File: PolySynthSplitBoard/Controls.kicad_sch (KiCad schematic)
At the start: 104 parts, among them SW601 ENV1_B, SW602 ENV2_B, SW603 HP_B, SW604 LFO1_B, SW605 LFO2_B, SW606 HP_B, SW607 LFO3_B, SW608 FF_B, SW609 MIX1_B, SW610 MIX2_B, SW611 ENC_MENU, SW612 ALT_B, U601 MCP23S17_SS, U602 MCP23S17_SS, U603 ILI9341

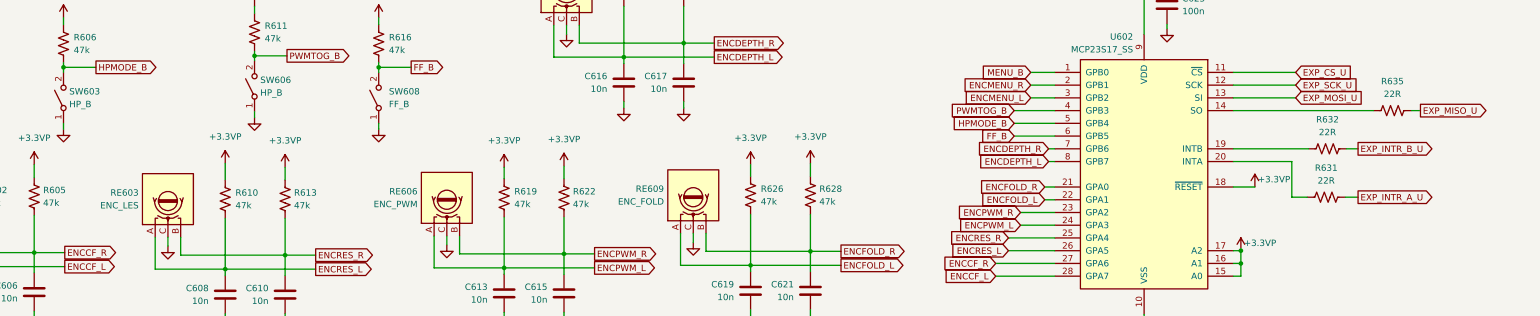
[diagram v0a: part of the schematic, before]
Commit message: upper board routing
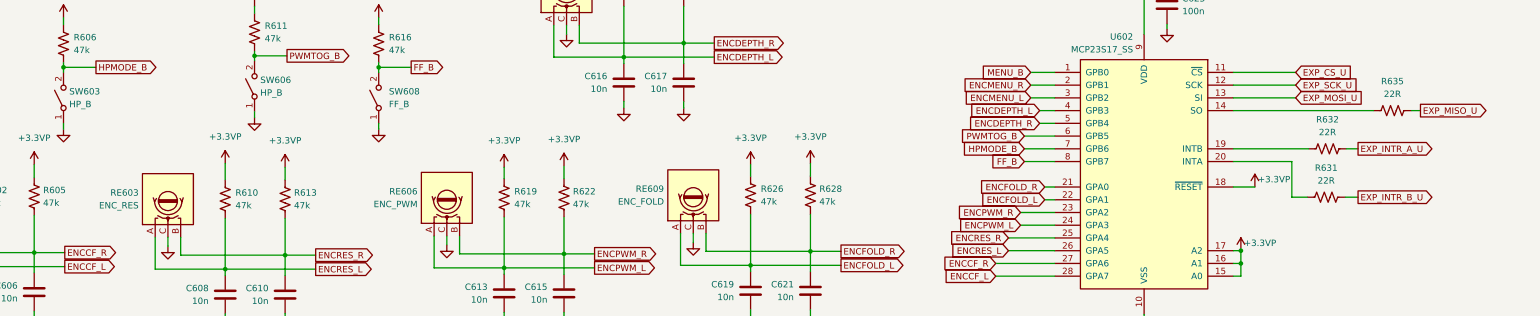
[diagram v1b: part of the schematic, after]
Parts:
- RE603: value ENC_LES -> ENC_RES
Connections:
- net ENCDEPTH_L: now also U602.4 (GPB3); no longer U602.8 (GPB7)
- net ENCDEPTH_R: now also U602.5 (GPB4); no longer U602.7 (GPB6)
- net EXP_INTR_A_U: now also R632.2; no longer R631.2
- net EXP_INTR_B_U: now also R631.2; no longer R632.2
- net FF_B: now also U602.8 (GPB7); no longer U602.6 (GPB5)
- net HPMODE_B: now also U602.7 (GPB6); no longer U602.5 (GPB4)
- net PWMTOG_B: now also U602.6 (GPB5); no longer U602.4 (GPB3)
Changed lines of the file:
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@@
 	(wire
 		(pts
-			(xy 246.634 183.896) (xy 254.762 183.896)
-		)
-		(stroke
-			(width 0)
-			(type default)
-		)
-	)
-	(wire
-		(pts
 			(xy 272.542 219.456) (xy 272.542 220.472)
 		)
@@
 	(wire
 		(pts
-			(xy 253.492 188.976) (xy 254.762 188.976)
-		)
-		(stroke
-			(width 0)
-			(type default)
-		)
-	)
-	(wire
-		(pts
 			(xy 224.79 83.312) (xy 229.108 83.312)
 		)
@@
 	(wire
 		(pts
+			(xy 248.666 186.436) (xy 254.762 186.436)
+		)
+		(stroke
+			(width 0)
+			(type default)
+		)
+	)
+	(wire
+		(pts
 			(xy 247.904 201.676) (xy 254.762 201.676)
 		)
@@
 	(wire
 		(pts
-			(xy 246.634 181.356) (xy 254.762 181.356)
+			(xy 251.714 181.356) (xy 254.762 181.356)
 		)
 		(stroke
@@
 	(wire
 		(pts
+			(xy 248.666 183.896) (xy 254.762 183.896)
+		)
+		(stroke
+			(width 0)
+			(type default)
+		)
+	)
+	(wire
+		(pts
 			(xy 175.26 101.346) (xy 175.26 107.696)
 		)
@@
 	(wire
 		(pts
+			(xy 248.666 188.976) (xy 254.762 188.976)
+		)
+		(stroke
+			(width 0)
+			(type default)
+		)
+	)
+	(wire
+		(pts
 			(xy 40.767 137.414) (xy 45.974 137.414)
 		)
@@
 	(wire
 		(pts
-			(xy 246.634 178.816) (xy 254.762 178.816)
+			(xy 251.714 178.816) (xy 254.762 178.816)
 		)
 		(stroke
@@
 	(wire
 		(pts
-			(xy 253.492 186.436) (xy 254.762 186.436)
-		)
-		(stroke
-			(width 0)
-			(type default)
-		)
-	)
-	(wire
-		(pts
 			(xy 322.326 83.82) (xy 322.326 85.598)
 		)
@@
 	(global_label "ENCDEPTH_R"
 		(shape input)
-		(at 253.492 186.436 180)
+		(at 251.714 181.356 180)
 		(fields_autoplaced yes)
 		(effects
@@
 		)
 		(property "Intersheetrefs" "${INTERSHEET_REFS}"
-			(at 238.7745 186.436 0)
+			(at 236.9965 181.356 0)
 			(effects
 				(font
@@
 	(global_label "ENCDEPTH_L"
 		(shape input)
-		(at 253.492 188.976 180)
+		(at 251.714 178.816 180)
 		(fields_autoplaced yes)
 		(effects
@@
 		)
 		(property "Intersheetrefs" "${INTERSHEET_REFS}"
-			(at 238.5326 188.976 0)
+			(at 236.7546 178.816 0)
 			(effects
 				(font
@@
 	(global_label "EXP_INTR_A_U"
 		(shape output)
-		(at 315.214 196.088 0)
+		(at 315.214 186.436 0)
 		(fields_autoplaced yes)
 		(effects
@@
 		)
 		(property "Intersheetrefs" "${INTERSHEET_REFS}"
-			(at 331.3225 196.088 0)
+			(at 331.3225 186.436 0)
 			(effects
 				(font
@@
 	(global_label "FF_B"
 		(shape input)
-		(at 246.634 183.896 180)
+		(at 248.666 188.976 180)
 		(fields_autoplaced yes)
 		(effects
@@
 		)
 		(property "Intersheetrefs" "${INTERSHEET_REFS}"
-			(at 239.234 183.896 0)
+			(at 241.266 188.976 0)
 			(effects
 				(font
@@
 	(global_label "EXP_INTR_B_U"
 		(shape output)
-		(at 315.214 186.436 0)
+		(at 315.214 196.088 0)
 		(fields_autoplaced yes)
 		(effects
@@
 		)
 		(property "Intersheetrefs" "${INTERSHEET_REFS}"
-			(at 331.5039 186.436 0)
+			(at 331.5039 196.088 0)
 			(effects
 				(font
@@
 	(global_label "PWMTOG_B"
 		(shape input)
-		(at 246.634 178.816 180)
+		(at 248.666 183.896 180)
 		(fields_autoplaced yes)
 		(effects
@@
 		)
 		(property "Intersheetrefs" "${INTERSHEET_REFS}"
-			(at 233.6703 178.816 0)
+			(at 235.7023 183.896 0)
 			(effects
 				(font
@@
 	(global_label "HPMODE_B"
 		(shape input)
-		(at 246.634 181.356 180)
+		(at 248.666 186.436 180)
 		(fields_autoplaced yes)
 		(effects
@@
 		)
 		(property "Intersheetrefs" "${INTERSHEET_REFS}"
-			(at 233.6098 181.356 0)
+			(at 235.6418 186.436 0)
 			(effects
 				(font
@@
 			)
 		)
-		(property "Value" "ENC_LES"
+		(property "Value" "ENC_RES"
 			(at 72.009 197.739 90)
 			(effects

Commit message: SPI and board tweaks
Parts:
- added C627: 10u, Capacitor_SMD:C_0805_2012Metric, symbol Device:C
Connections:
- net +3.3VP: now also C627.1
- net GNDA: now also C627.2
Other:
- moved on the sheet: C626
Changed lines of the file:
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@@
 	)
 	(junction
-		(at 363.728 27.178)
-		(diameter 0)
-		(color 0 0 0 0)
-	)
-	(junction
 		(at 88.519 63.5)
 		(diameter 0)
@@
 	)
 	(junction
+		(at 374.396 27.432)
+		(diameter 0)
+		(color 0 0 0 0)
+	)
+	(junction
 		(at 318.77 57.658)
 		(diameter 0)
@@
 	)
 	(junction
+		(at 363.728 27.432)
+		(diameter 0)
+		(color 0 0 0 0)
+	)
+	(junction
 		(at 95.123 167.894)
 		(diameter 0)
@@
 	(wire
 		(pts
-			(xy 363.728 27.178) (xy 363.728 38.608)
+			(xy 363.728 26.416) (xy 363.728 27.432)
 		)
 		(stroke
@@
 	(wire
 		(pts
+			(xy 363.728 27.432) (xy 363.728 38.608)
+		)
+		(stroke
+			(width 0)
+			(type default)
+		)
+	)
+	(wire
+		(pts
 			(xy 227.076 60.452) (xy 229.108 60.452)
 		)
@@
 	(wire
 		(pts
+			(xy 385.572 27.432) (xy 374.396 27.432)
+		)
+		(stroke
+			(width 0)
+			(type default)
+		)
+	)
+	(wire
+		(pts
 			(xy 51.181 87.249) (xy 51.181 89.916)
 		)
@@
 	(wire
 		(pts
+			(xy 385.572 36.83) (xy 385.572 37.592)
+		)
+		(stroke
+			(width 0)
+			(type default)
+		)
+	)
+	(wire
+		(pts
 			(xy 201.168 116.586) (xy 201.168 117.856)
 		)
@@
 	(wire
 		(pts
-			(xy 359.41 27.178) (xy 363.728 27.178)
-		)
-		(stroke
-			(width 0)
-			(type default)
-		)
-	)
-	(wire
-		(pts
 			(xy 180.721 165.354) (xy 186.817 165.354)
 		)
@@
 	(wire
 		(pts
+			(xy 374.396 27.432) (xy 374.396 29.21)
+		)
+		(stroke
+			(width 0)
+			(type default)
+		)
+	)
+	(wire
+		(pts
 			(xy 180.721 177.038) (xy 180.721 178.308)
 		)
@@
 	(wire
 		(pts
+			(xy 374.396 27.432) (xy 363.728 27.432)
+		)
+		(stroke
+			(width 0)
+			(type default)
+		)
+	)
+	(wire
+		(pts
 			(xy 189.23 116.586) (xy 189.23 117.856)
 		)
@@
 	(wire
 		(pts
-			(xy 359.41 36.068) (xy 359.41 36.83)
+			(xy 374.396 36.83) (xy 374.396 37.592)
 		)
 		(stroke
@@
 	(wire
 		(pts
+			(xy 385.572 29.21) (xy 385.572 27.432)
+		)
+		(stroke
+			(width 0)
+			(type default)
+		)
+	)
+	(wire
+		(pts
 			(xy 80.899 24.765) (xy 80.899 25.654)
 		)
@@
 	(wire
 		(pts
-			(xy 359.41 28.448) (xy 359.41 27.178)
-		)
-		(stroke
-			(width 0)
-			(type default)
-		)
-	)
-	(wire
-		(pts
 			(xy 127.254 74.803) (xy 127.254 75.946)
 		)
@@
 	(wire
 		(pts
-			(xy 363.728 26.416) (xy 363.728 27.178)
-		)
-		(stroke
-			(width 0)
-			(type default)
-		)
-	)
-	(wire
-		(pts
 			(xy 88.646 104.394) (xy 109.474 104.394)
 		)
@@
 	(symbol
 		(lib_id "Device:C")
-		(at 359.41 32.258 0)
+		(at 374.396 33.02 0)
 		(unit 1)
 		(exclude_from_sim no)
@@
 		(dnp no)
 		(property "Reference" "C626"
-			(at 356.108 30.988 0)
+			(at 371.094 31.75 0)
 			(effects
 				(font
@@
 		)
 		(property "Value" "100n"
-			(at 356.108 33.528 0)
+			(at 371.094 34.29 0)
 			(effects
 				(font
@@
 		)
 		(property "Footprint" "Capacitor_SMD:C_0805_2012Metric"
-			(at 360.3752 36.068 0)
+			(at 375.3612 36.83 0)
 			(effects
 				(font
@@
 		)
 		(property "Datasheet" "~"
-			(at 359.41 32.258 0)
+			(at 374.396 33.02 0)
 			(effects
 				(font
@@
 		)
 		(property "Description" ""
-			(at 359.41 32.258 0)
+			(at 374.396 33.02 0)
 			(effects
 				(font
@@
 	(symbol
 		(lib_id "power:GND")
-		(at 359.41 36.83 0)
+		(at 374.396 37.592 0)
 		(unit 1)
 		(exclude_from_sim no)
@@
 		(fields_autoplaced yes)
 		(property "Reference" "#PWR0765"
-			(at 359.41 43.18 0)
+			(at 374.396 43.942 0)
 			(effects
 				(font
@@
 		)
 		(property "Value" "GNDA"
-			(at 359.41 40.64 0)
+			(at 374.396 41.402 0)
 			(effects
 				(font
@@
 		)
 		(property "Footprint" ""
-			(at 359.41 36.83 0)
+			(at 374.396 37.592 0)
 			(effects
 				(font
@@
 		)
 		(property "Datasheet" ""
-			(at 359.41 36.83 0)
+			(at 374.396 37.592 0)
 			(effects
 				(font
@@
 		)
 		(property "Description" ""
-			(at 359.41 36.83 0)
+			(at 374.396 37.592 0)
 			(effects
 				(font
@@
 	)
 	(symbol
+		(lib_id "Device:C")
+		(at 385.572 33.02 0)
+		(unit 1)
+		(exclude_from_sim no)
+		(in_bom yes)
+		(on_board yes)
+		(dnp no)
+		(property "Reference" "C627"
+			(at 382.27 31.75 0)
+			(effects
+				(font
+					(size 1.27 1.27)
+				)
+				(justify right)
+			)
+		)
+		(property "Value" "10u"
+			(at 382.27 34.29 0)
+			(effects
+				(font
+					(size 1.27 1.27)
+				)
+				(justify right)
+			)
+		)
+		(property "Footprint" "Capacitor_SMD:C_0805_2012Metric"
+			(at 386.5372 36.83 0)
+			(effects
+				(font
+					(size 1.27 1.27)
+				)
+				(hide yes)
+			)
+		)
+		(property "Datasheet" "~"
+			(at 385.572 33.02 0)
+			(effects
+				(font
+					(size 1.27 1.27)
+				)
+				(hide yes)
+			)
+		)
+		(property "Description" ""
+			(at 385.572 33.02 0)
+			(effects
+				(font
+					(size 1.27 1.27)
+				)
+				(hide yes)
+			)
+		)
+		(pin "1"
+		)
+		(pin "2"
+		)
+		(instances
+			(project "PolySynthSplitBoard"
+				(path "/22649217-9810-470f-bc7b-6f743ad2b90e/db382c1e-7a8e-4aae-96bd-96ec756a5476/f9611335-018a-4682-8f39-2088bfa85de9"
+					(reference "C627")
+					(unit 1)
+				)
+			)
+		)
+	)
+	(symbol
 		(lib_id "power:GND")
 		(at 27.813 205.359 0)
@@
 					(unit 1)
 				)
+			)
+		)
+	)
+	(symbol
+		(lib_id "power:GND")
+		(at 385.572 37.592 0)
+		(unit 1)
+		(exclude_from_sim no)
+		(in_bom yes)
+		(on_board yes)
+		(dnp no)
+		(fields_autoplaced yes)
+		(property "Reference" "#PWR0839"
+			(at 385.572 43.942 0)
+			(effects
+				(font
+					(size 1.27 1.27)
+				)
+				(hide yes)
+			)
+		)
+		(property "Value" "GNDA"
+			(at 385.572 41.402 0)
+			(effects
+				(font
+					(size 1.27 1.27)
+				)
+				(hide yes)
+			)
+		)
+		(property "Footprint" ""
+			(at 385.572 37.592 0)
+			(effects
+				(font
+					(size 1.27 1.27)
+				)
+				(hide yes)
+			)
+		)
+		(property "Datasheet" ""
+			(at 385.572 37.592 0)
+			(effects
+				(font
+					(size 1.27 1.27)
+				)
+				(hide yes)
+			)
+		)
+		(property "Description" ""
+			(at 385.572 37.592 0)
+			(effects
+				(font
+					(size 1.27 1.27)
+				)
+				(hide yes)
+			)
+		)
+		(pin "1"
+		)
+		(instances
+			(project "PolySynthSplitBoard"
+				(path "/22649217-9810-470f-bc7b-6f743ad2b90e/db382c1e-7a8e-4aae-96bd-96ec756a5476/f9611335-018a-4682-8f39-2088bfa85de9"
+					(reference "#PWR0839")
+					(unit 1)
+				)

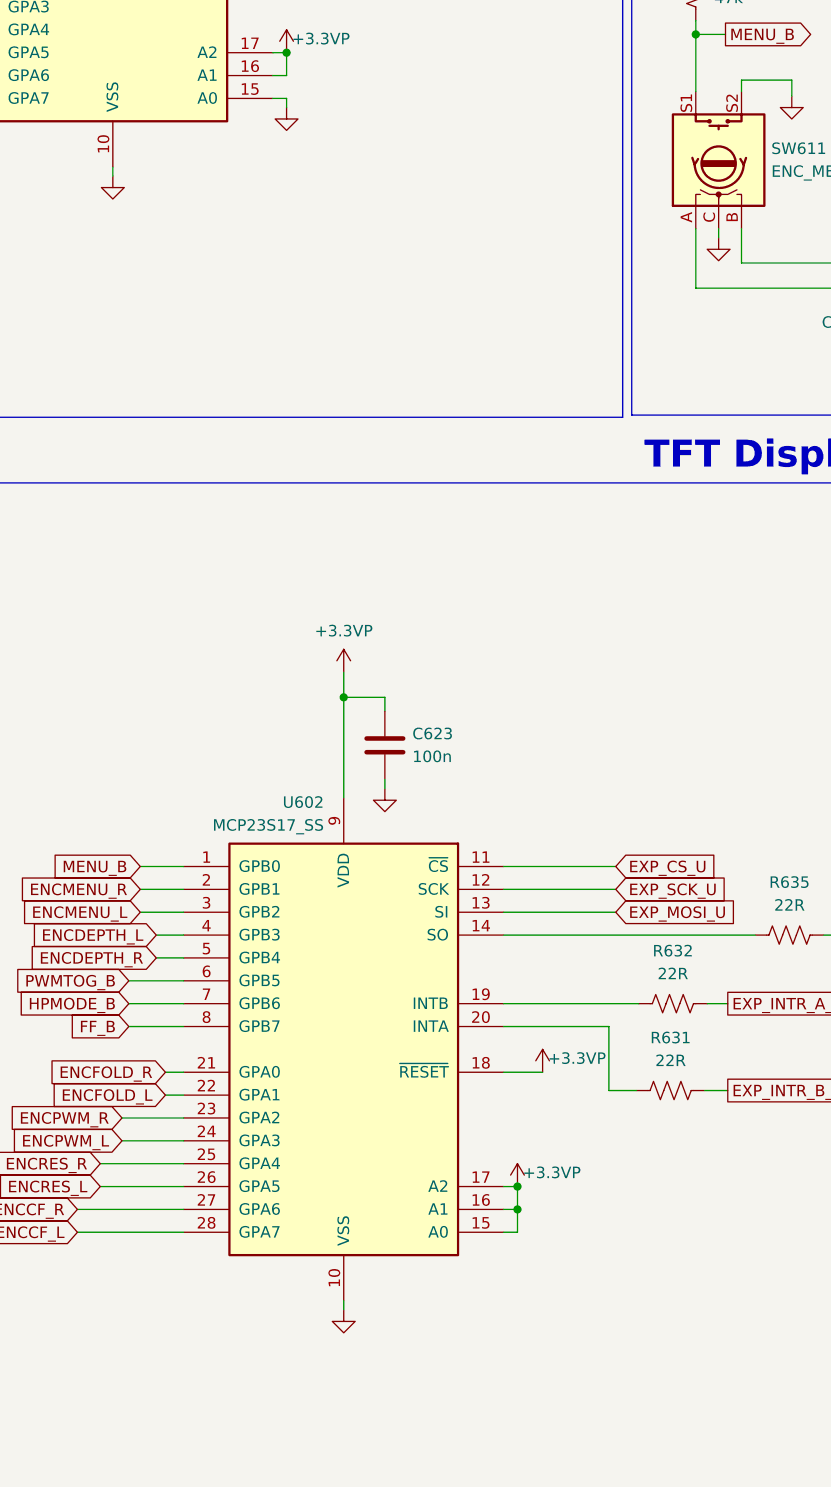
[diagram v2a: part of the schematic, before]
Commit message: Button indeces and mapping
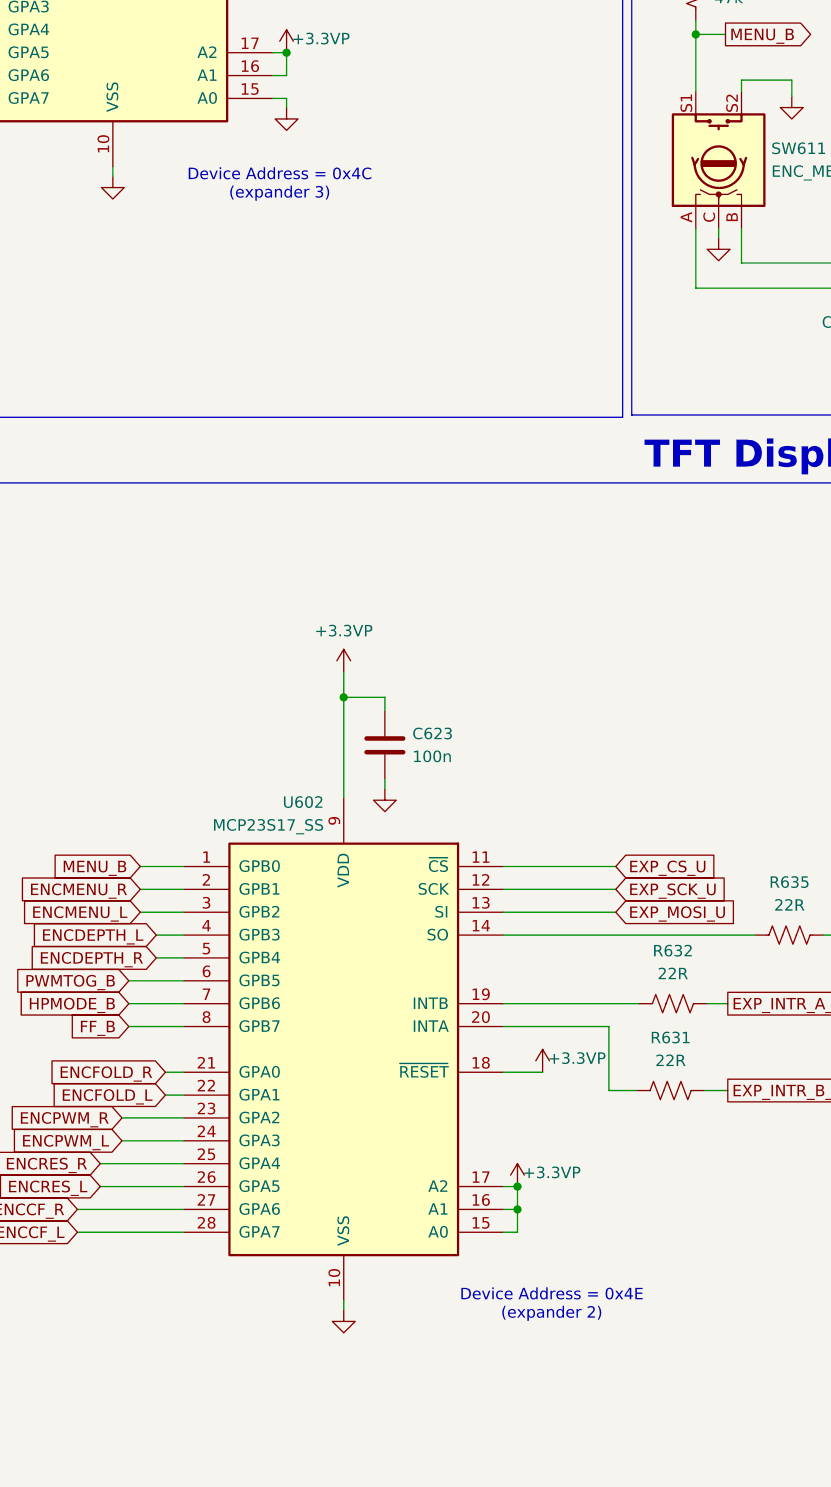
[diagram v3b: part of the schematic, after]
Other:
- note added: "Device Address = 0x4C (expander 3)"
- note added: "Device Address = 0x4E (expander 2)"
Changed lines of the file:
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@@
+		)
+	)
+	(text "Device Address = 0x4E\n(expander 2)"
+		(exclude_from_sim no)
+		(at 295.656 219.964 0)
+		(effects
+			(font
+				(size 1.27 1.27)
+			)
+		)
+	)
+	(text "Device Address = 0x4C\n(expander 3)"
+		(exclude_from_sim no)
+		(at 265.43 95.504 0)
+		(effects
+			(font
+				(size 1.27 1.27)
+			)
 		)
 	)
